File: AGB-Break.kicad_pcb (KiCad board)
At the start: 2 copper layers, 74.4 x 86.7 mm, 70 parts, among them J1 CONN_WII, J2 Conn_02x03_Odd_Even, J3 Conn_01x02, J4 GameBoy_LinkPort, SW1 SW_Push, U1 AGB-CPU, U2 ATmega328PB-AU, U3 TS5A3160DBV, U4 AGB_SRAM, U5 SpartanEdge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

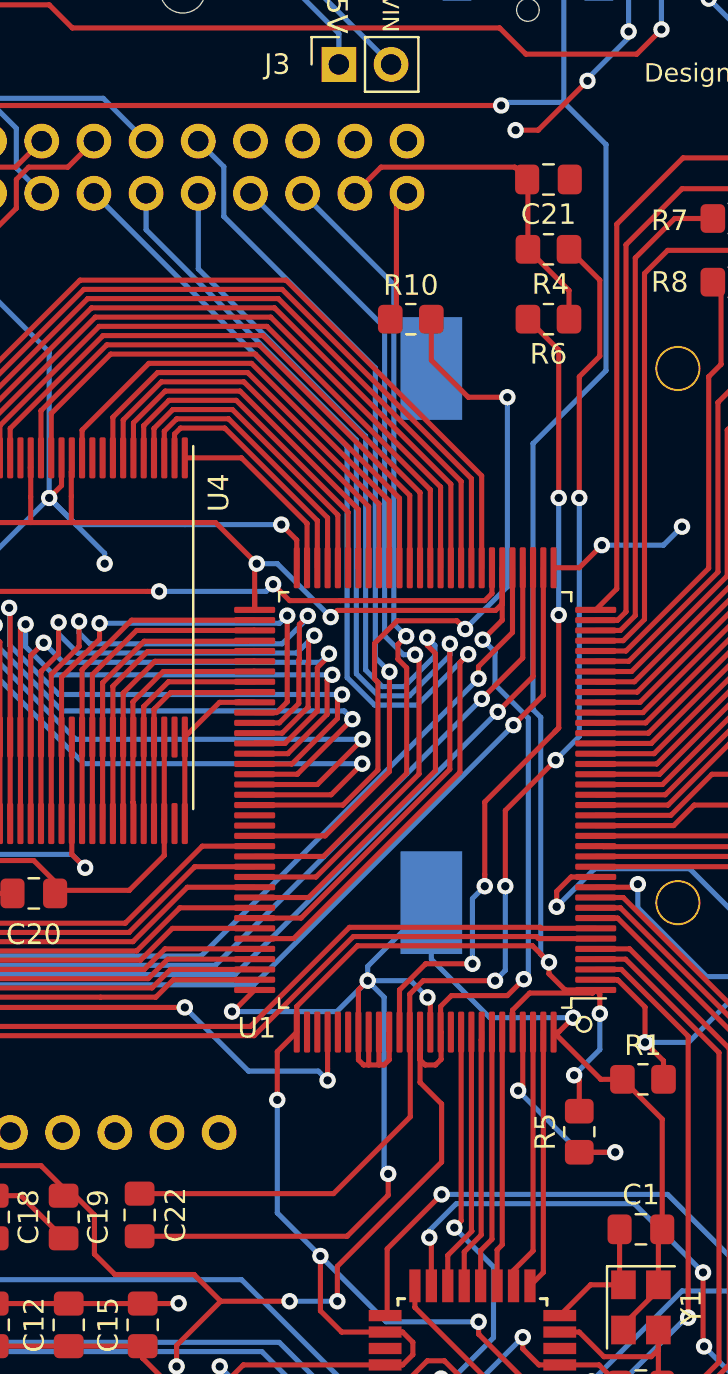
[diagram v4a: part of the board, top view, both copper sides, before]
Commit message: Changed clock wiring
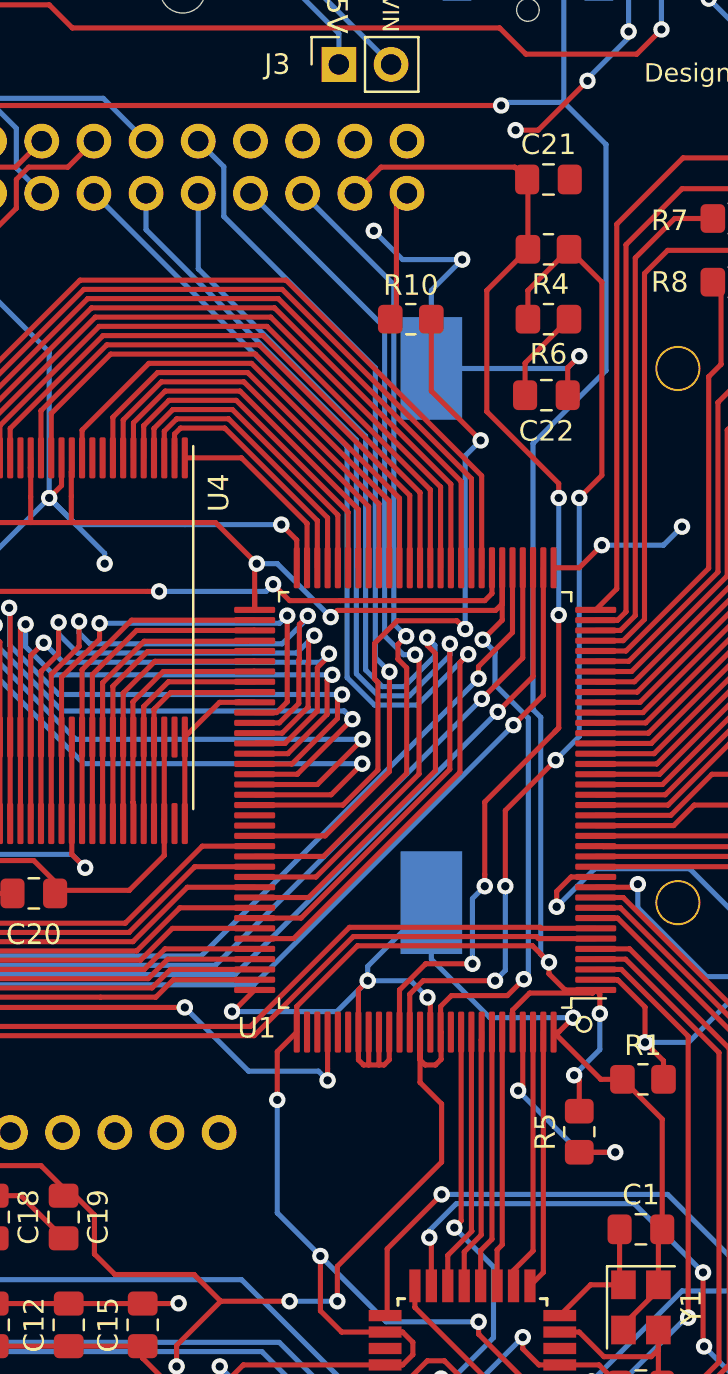
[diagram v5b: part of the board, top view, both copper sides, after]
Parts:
- moved C22 44.5 mm to (185.9, 60.9), turned to 0 degrees
- turned C21 to 180 degrees
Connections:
- C21 pad 1: GBA_CLK -> GND
- C21 pad 2: GND -> GBA_CLK
- C22 pad 1: GND -> Net-(C22-Pad1)
- C22 pad 2: Net-(C22-Pad2) -> GND
- R4 pad 2: Net-(C22-Pad2) -> Net-(R4-Pad2)
- R6 pad 1: Net-(R6-Pad1) -> Net-(R4-Pad2)
- R6 pad 2: GBA_CLK -> Net-(C22-Pad1)
- U1 pad 113: Net-(R6-Pad1) -> GBA_CLK
- U1 pad 114: Net-(C22-Pad2) -> Net-(R4-Pad2)
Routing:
- net Net-(C22-Pad2): track 63.8 -> 0.00 mm, vias 4 -> 0
- net Net-(R4-Pad2): track 0.00 -> 49.2 mm, vias 0 -> 4
- net GBA_CLK: track 16.8 -> 57.8 mm, vias 0 -> 4
- net Net-(R6-Pad1): track 40.1 -> 0.00 mm, vias 4 -> 0
- net Net-(C22-Pad1): track 0.00 -> 4.59 mm
- net GND: track 406.1 -> 402.7 mm, vias 35 -> 37
- net Net-(R10-Pad2): track 36.5 -> 34.4 mm
